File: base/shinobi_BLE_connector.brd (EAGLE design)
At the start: 40.5 x 35 mm, 19 parts

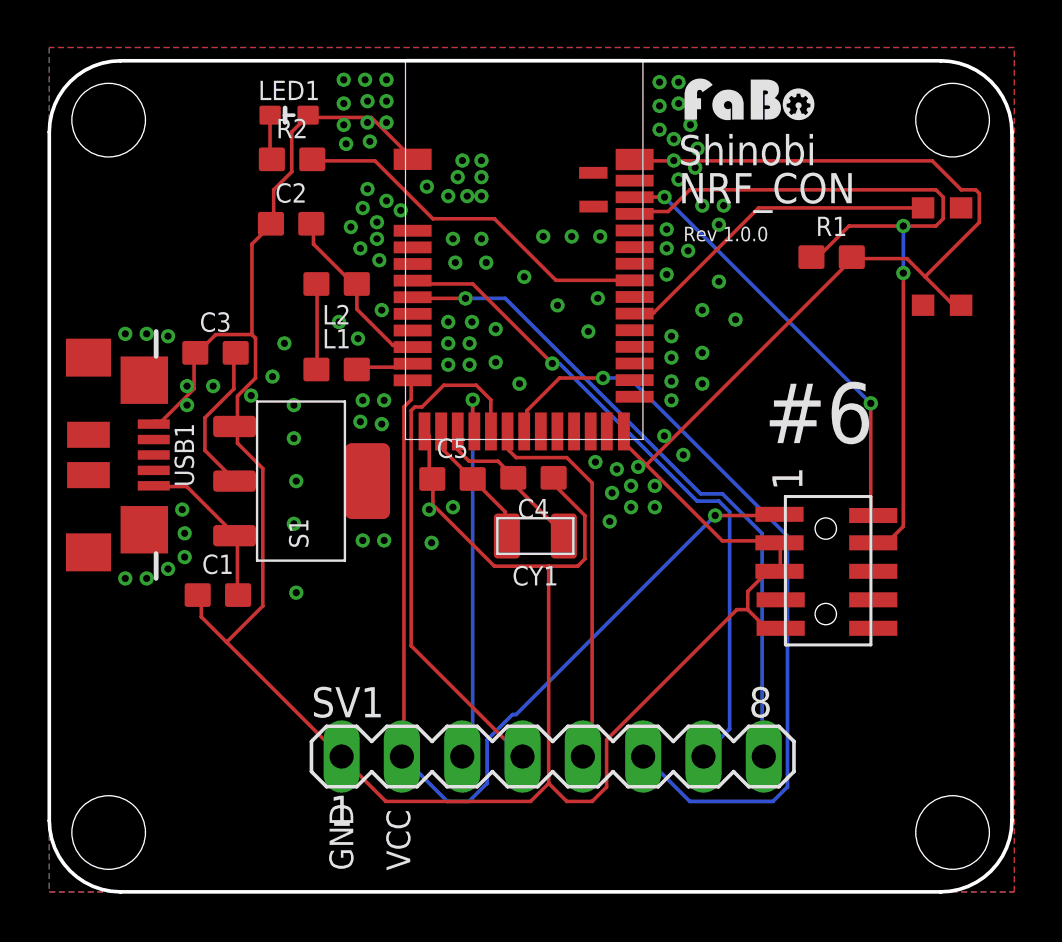
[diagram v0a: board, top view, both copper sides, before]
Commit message: Add shinobi connector.
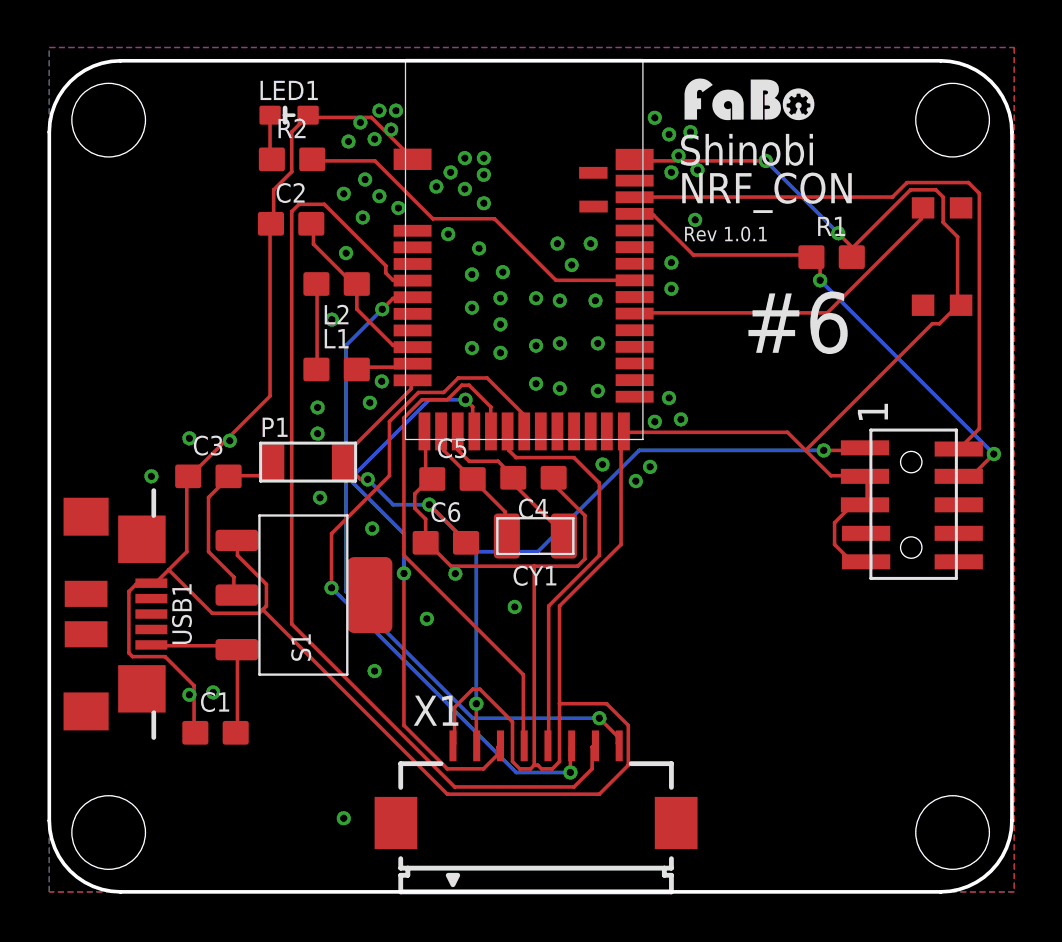
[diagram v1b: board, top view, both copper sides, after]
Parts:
- removed SV1: (no value), con-lstb:MA08-1
- added C6: 0.1uF, FaBo-Capacitor:0603
- added P1: MF-NSML600-2, FaBo-Supply:1206
- added X1: FH12-08S-1SH, con-hirose:FH12-08S-1SH
- moved USB1 6.70 mm to (0.10, 11.7)
- moved C1 5.80 mm to (7.00, 6.70)
- moved C3 5.21 mm to (6.70, 17.5)
- moved S1 4.80 mm to (10.7, 12.5)
- moved U$4 4.56 mm to (36.3, 16.3)
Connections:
- removed net 3V3: C3.2, S1.2
- new net N$5: C3.2, P1.P$1, S1.2
- net +3V3: now also C6.2, P1.P$2, X1.2; no longer SV1.2
- net GND: now also C6.1, X1.1; no longer SV1.1
- net P0.02: now also X1.3; no longer SV1.3
- net P0.03: now also X1.4; no longer SV1.4
- net P0.04: now also X1.5; no longer SV1.5
- net P0.05: now also X1.6; no longer SV1.6
- net P0.28: now also X1.7; no longer SV1.7
- net P0.29: now also X1.8; no longer SV1.8
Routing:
- net GND: track 144.4 -> 165.0 mm, vias 118 -> 74
- net SWCLK: track 34.9 -> 21.5 mm
- net P0.28: track 28.2 -> 41.0 mm, vias 1 -> 0
- net N$5: track 0.00 -> 7.93 mm
- net SWDIO: track 18.3 -> 26.1 mm, vias 2 -> 0
- net P0.02: track 16.6 -> 24.3 mm, vias 1 -> 2
- net 3V3: track 6.43 -> 0.00 mm
- net P0.05: track 32.9 -> 30.2 mm, vias 1 -> 2
- net +3V3: track 38.8 -> 40.4 mm, vias 1 -> 4
- net P0.04: track 16.6 -> 17.2 mm
- net P0.29: track 28.2 -> 28.4 mm, vias 1 -> 2
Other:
- board text added: "Rev 1.0.1"
- board text removed: "GND"
- board text removed: "Rev 1.0.0"
- board text removed: "VCC"

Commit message: Update.
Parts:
- removed R1: (no value), FaBo-Resistors:0603
- CY1: value (none) -> 32KHz
- L1: value 10nh -> 10uh
- R2: value (none) -> 220
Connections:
- net GND: no longer R1.2
- net SWCLK: no longer R1.1
